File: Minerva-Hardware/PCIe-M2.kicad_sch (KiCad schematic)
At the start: 20 parts, among them J1 Bus_M.2_Socket_M, M6 M.2 Solder Nut, M7 M.2 Screw, U2 ASEK-32.768KHZ-L-R-T, U8 AP3441SHE-7B

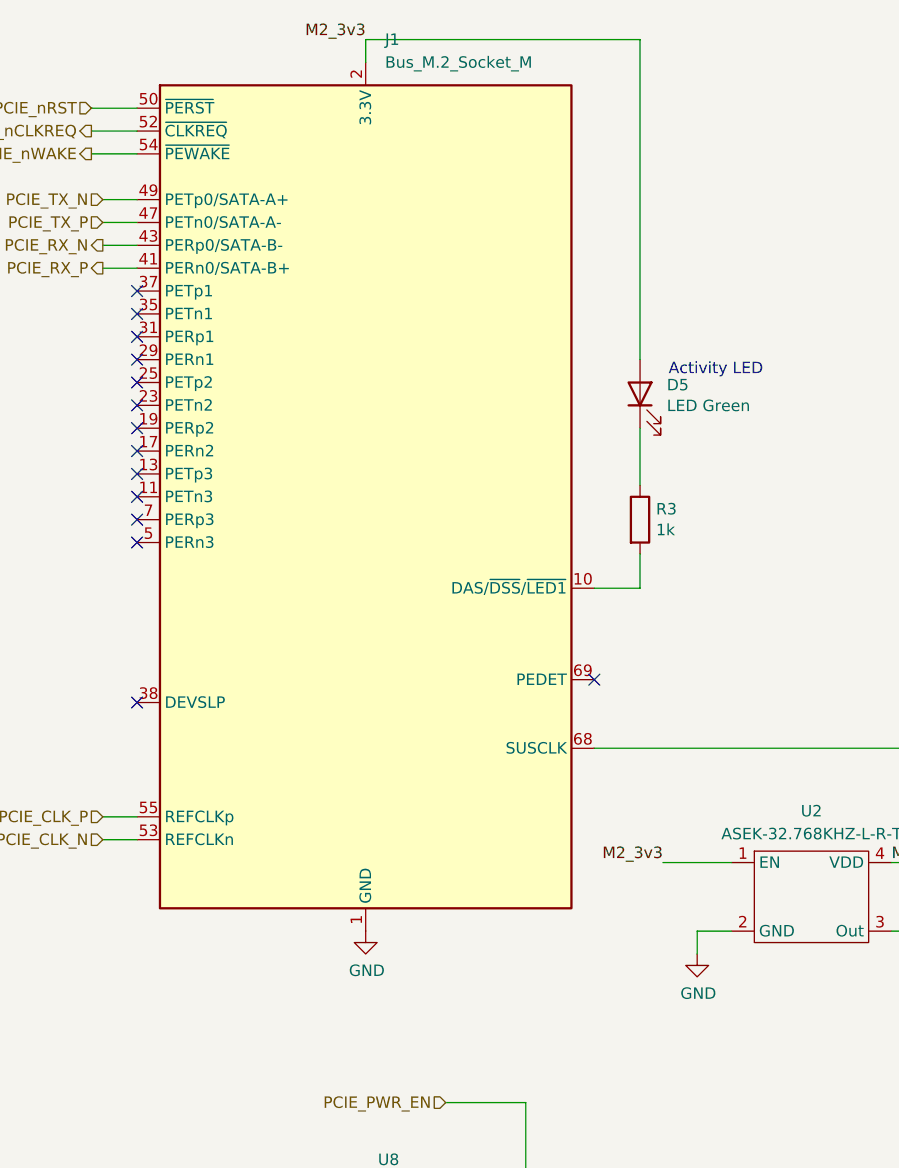
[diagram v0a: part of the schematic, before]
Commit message: Rename and commit actions due to mishap of location naming/saving
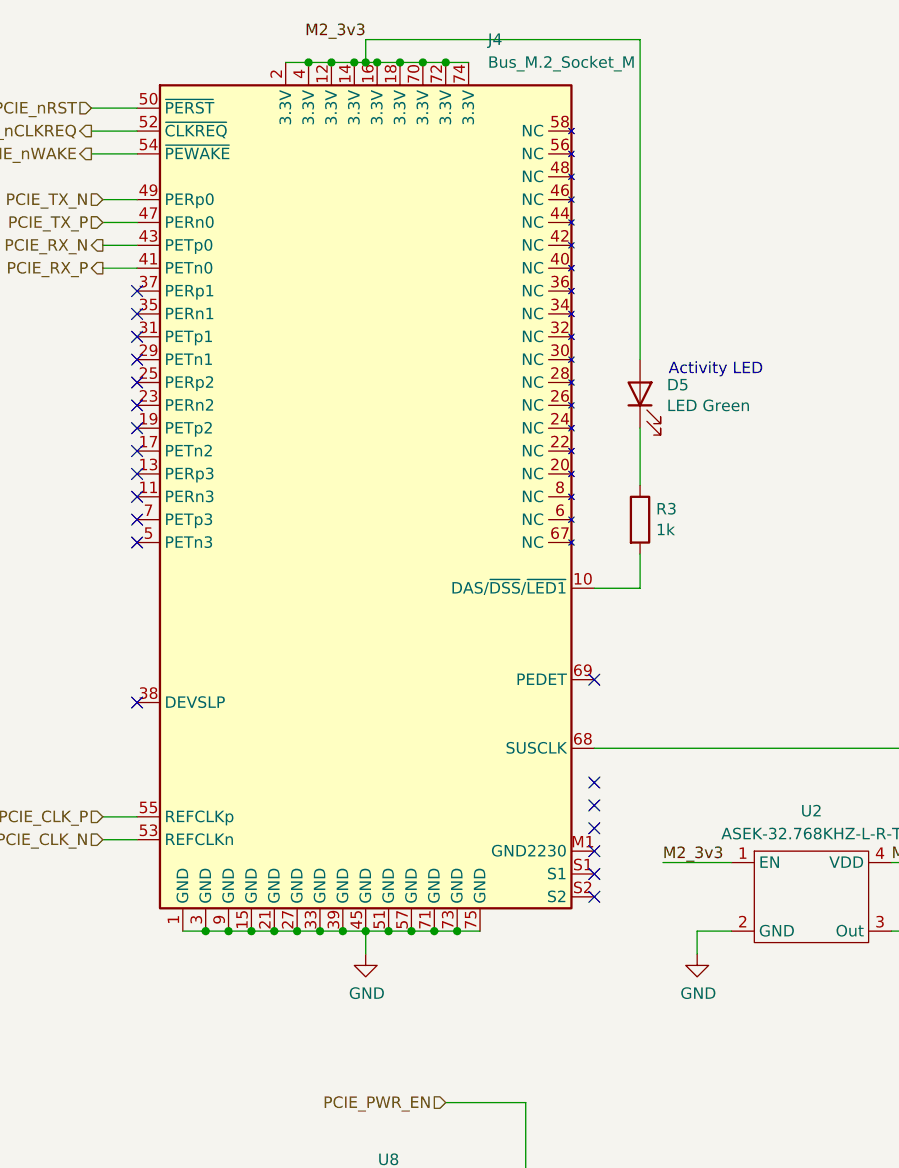
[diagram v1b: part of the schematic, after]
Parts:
- removed J1: Bus_M.2_Socket_M, Connector_PCBEdge:M.2_2242-xx-M, symbol Connector:Bus_M.2_Socket_M
- added J4: Bus_M.2_Socket_M, CM5 IO Board-rev2:M.2 M Key socket 2230, symbol CM5IO:Bus_M.2_Socket_M
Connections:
- net GND: now also J4.1 (GND), J4.15 (GND), J4.21 (GND), J4.27 (GND), J4.3 (GND), J4.33 (GND), J4.39 (GND), J4.45 (GND), J4.51 (GND), J4.57 (GND), J4.71 (GND), J4.73 (GND), J4.75 (GND), J4.9 (GND)
- net M2_3v3: now also J4.12 (3.3V), J4.14 (3.3V), J4.16 (3.3V), J4.18 (3.3V), J4.2 (3.3V), J4.4 (3.3V), J4.70 (3.3V), J4.72 (3.3V), J4.74 (3.3V)
- net PCIE_CLK_N: now also J4.53 (REFCLKn)
- net PCIE_CLK_P: now also J4.55 (REFCLKp)
- net PCIE_RX_N: now also J4.43 (PETp0)
- net PCIE_RX_P: now also J4.41 (PETn0)
- net PCIE_TX_N: now also J4.49 (PERp0)
- net PCIE_TX_P: now also J4.47 (PERn0)
- net PCIE_nCLKREQ: now also J4.52 (~{CLKREQ})
- net PCIE_nRST: now also J4.50 (~{PERST})
- net PCIE_nWAKE: now also J4.54 (~{PEWAKE})
- net at R3.2: now also J4.10 (DAS/~{DSS}/~{LED1})
- net at U2.3 (Out): now also J4.68 (SUSCLK)
- no-connect marks 15 -> 21

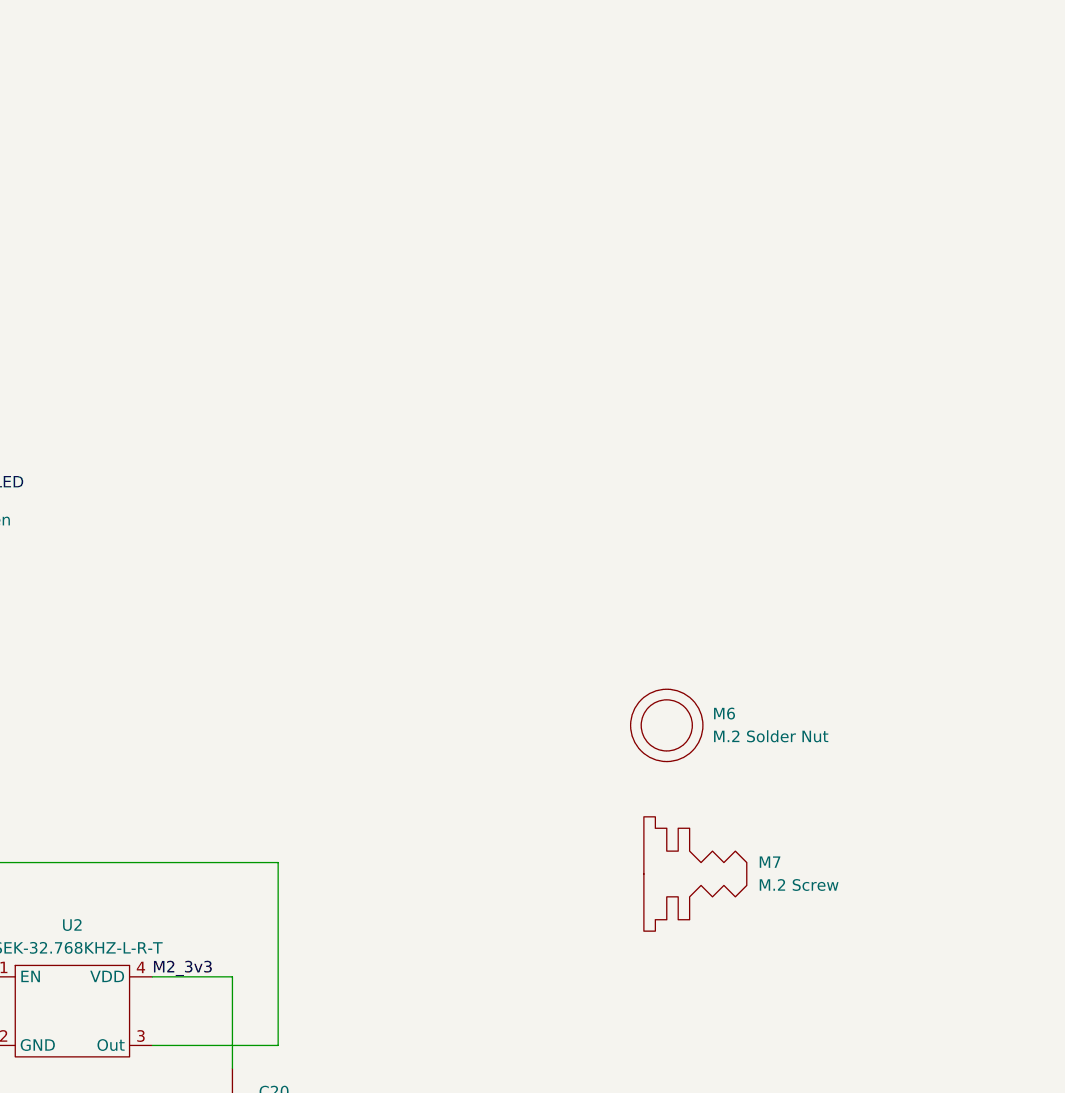
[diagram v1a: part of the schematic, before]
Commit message: Adding MiniPCI-E stuff
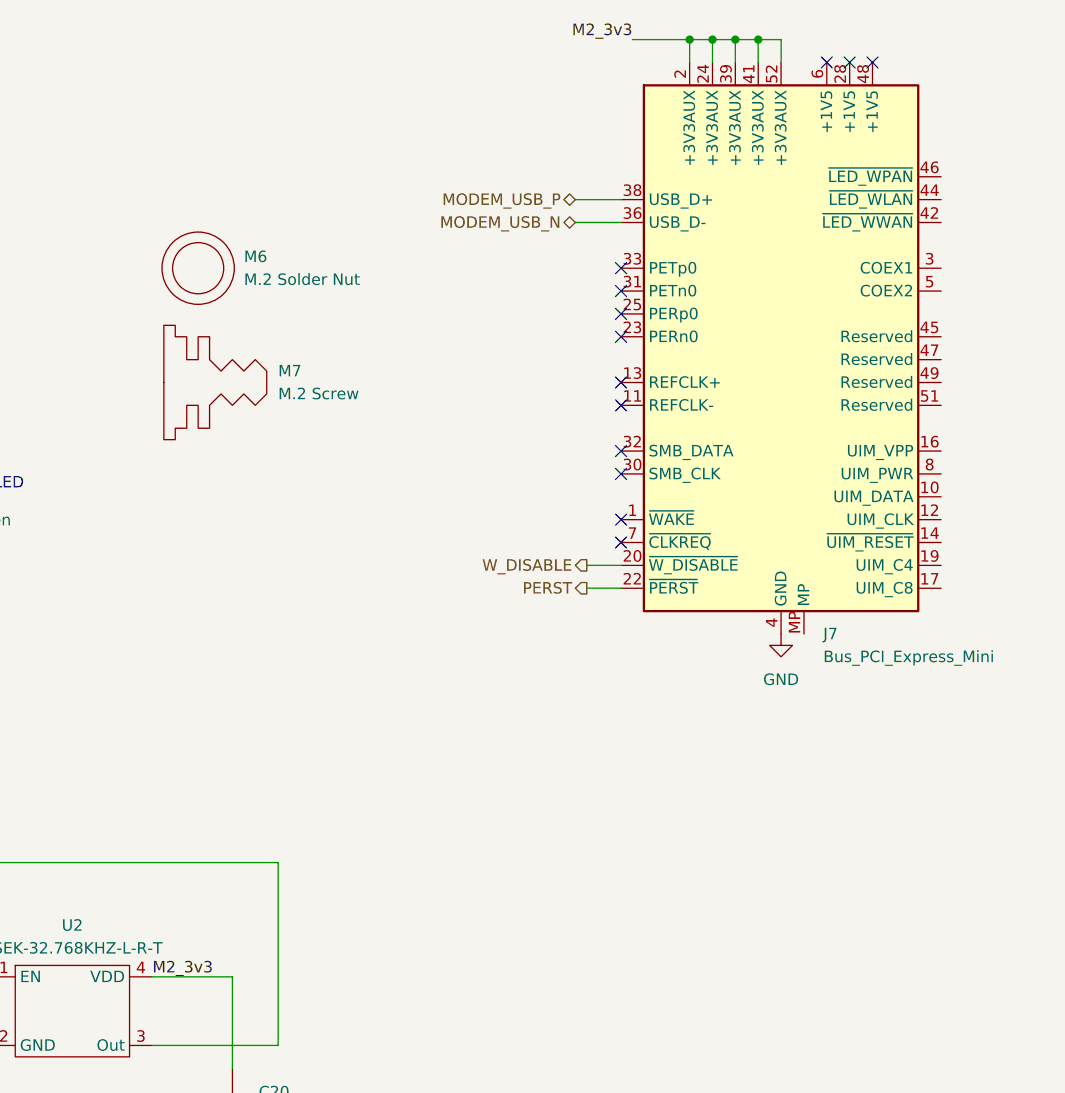
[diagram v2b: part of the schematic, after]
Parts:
- added J7: Bus_PCI_Express_Mini, symbol Connector:Bus_PCI_Express_Mini
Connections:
- net GND: now also J7.15 (GND), J7.18 (GND), J7.21 (GND), J7.26 (GND), J7.27 (GND), J7.29 (GND), J7.34 (GND), J7.35 (GND), J7.37 (GND), J7.4 (GND), J7.40 (GND), J7.43 (GND), J7.50 (GND), J7.9 (GND)
- net M2_3v3: now also J7.2 (+3V3AUX), J7.24 (+3V3AUX), J7.39 (+3V3AUX), J7.41 (+3V3AUX), J7.52 (+3V3AUX)
- new net MODEM_USB_N: J7.36 (USB_D-)
- new net MODEM_USB_P: J7.38 (USB_D+)
- new net PERST: J7.22 (~{PERST})
- new net W_DISABLE: J7.20 (~{W_DISABLE})
- no-connect marks 21 -> 34
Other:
- moved on the sheet: M6, M7

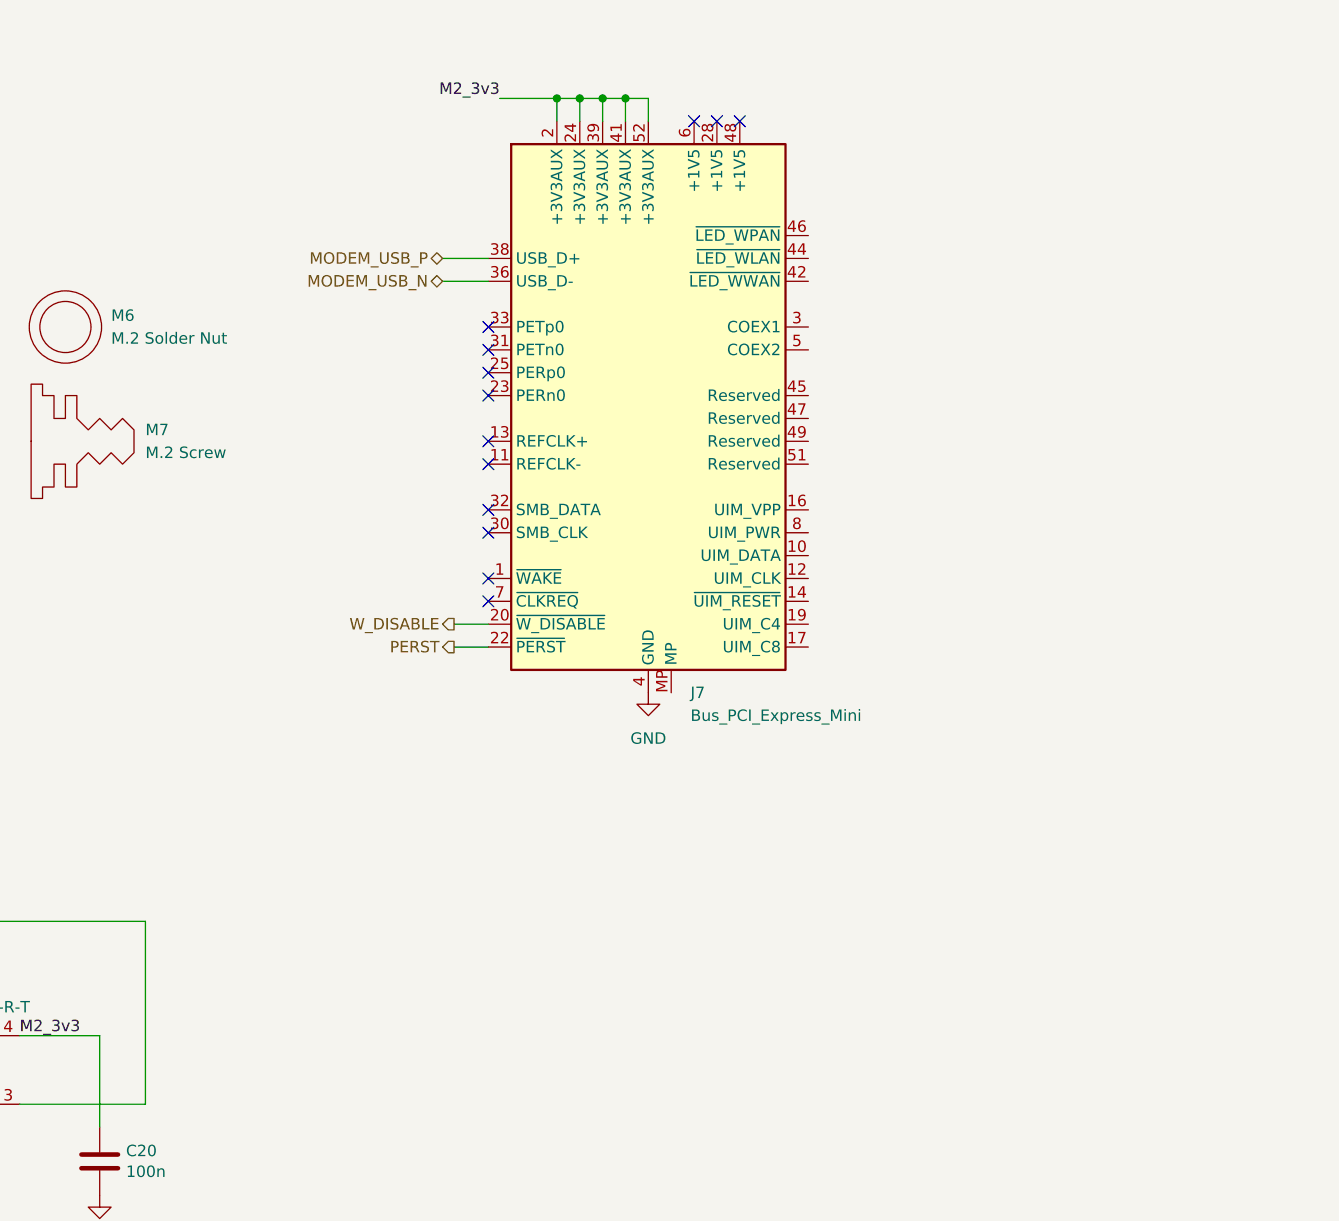
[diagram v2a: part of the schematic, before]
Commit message: Adding in the M.2 B WWAN
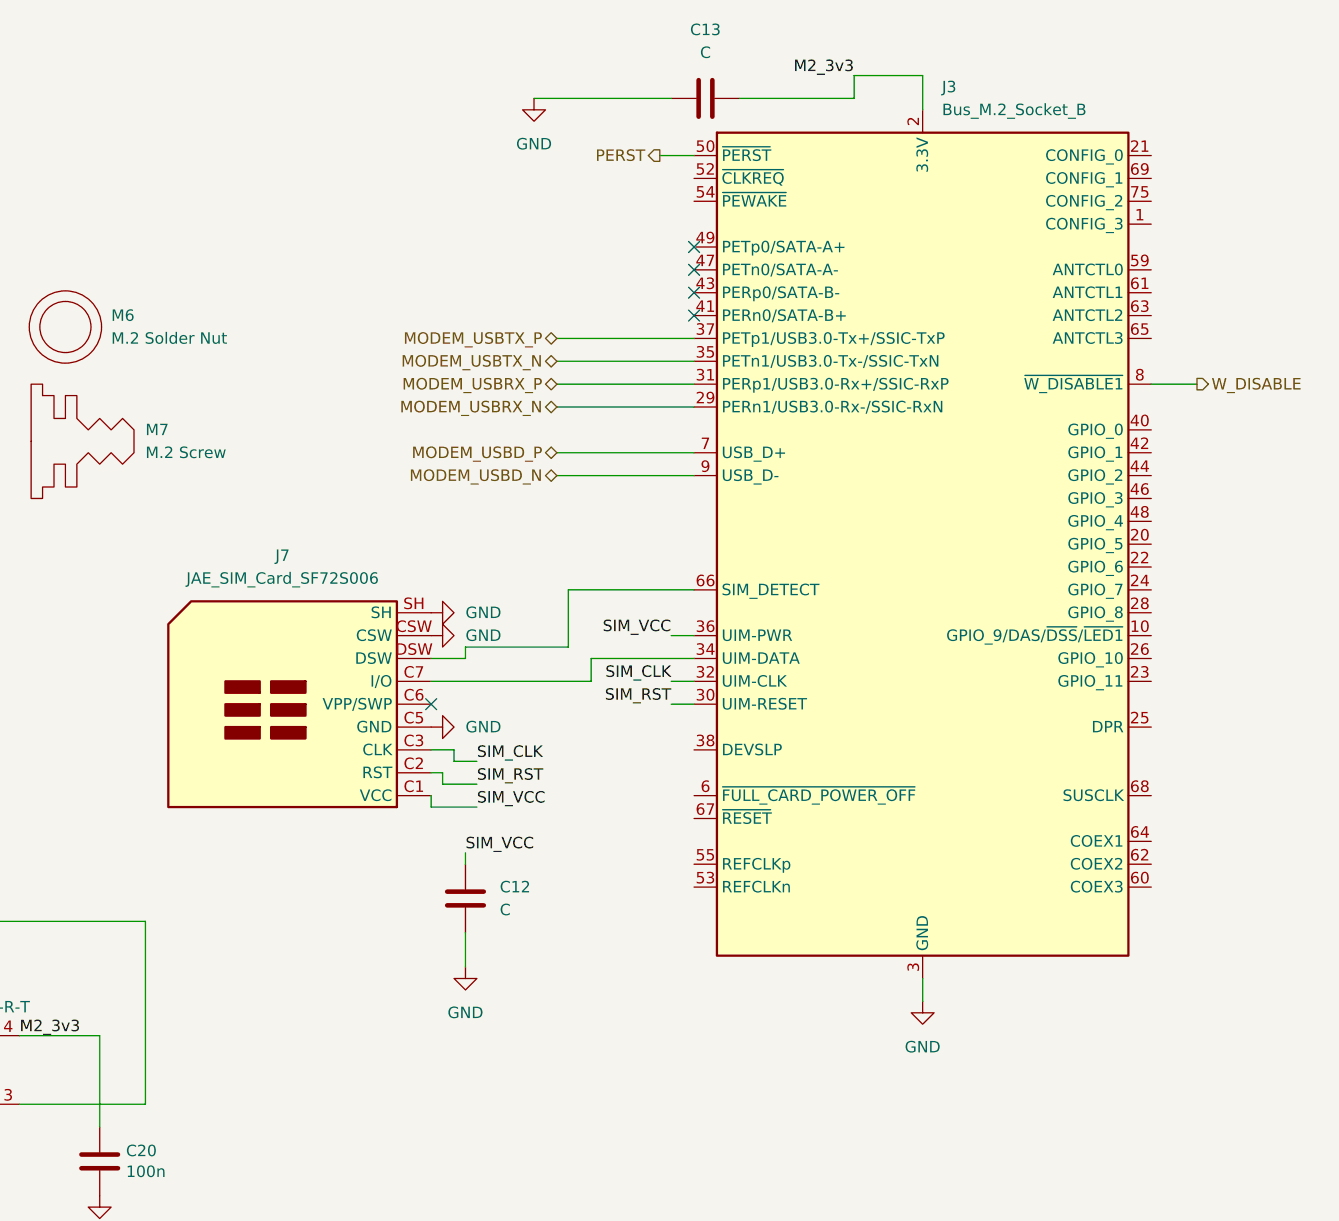
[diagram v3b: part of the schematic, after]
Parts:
- removed J7: Bus_PCI_Express_Mini, symbol Connector:Bus_PCI_Express_Mini
- added C12, C13: C, symbol Device:C
- added J3: Bus_M.2_Socket_B, Connector_PCBEdge:M.2_3042-xx-B, symbol Connector:Bus_M.2_Socket_B
- added J7: JAE_SIM_Card_SF72S006, Connector_JAE:JAE_SIM_Card_SF72S006, symbol Connector:JAE_SIM_Card_SF72S006
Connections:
- net GND: now also C12.2, C13.1, J3.11 (GND), J3.27 (GND), J3.3 (GND), J3.33 (GND), J3.39 (GND), J3.45 (GND), J3.5 (GND), J3.51 (GND), J3.57 (GND), J3.71 (GND), J3.73 (GND), J7.C5 (GND), J7.CSW, J7.SH
- net M2_3v3: now also C13.2, J3.2 (3.3V), J3.4 (3.3V), J3.70 (3.3V), J3.72 (3.3V), J3.74 (3.3V)
- net PERST: now also J3.50 (~{PERST})
- net W_DISABLE: now also J3.8 (~{W_DISABLE1})
- new net: J3.34 (UIM-DATA), J7.C7 (I/O)
- new net: J3.66 (SIM_DETECT), J7.DSW
- new net MODEM_USBD_N: J3.9 (USB_D-)
- new net MODEM_USBD_P: J3.7 (USB_D+)
- new net MODEM_USBRX_N: J3.29 (PERn1/USB3.0-Rx-/SSIC-RxN)
- new net MODEM_USBRX_P: J3.31 (PERp1/USB3.0-Rx+/SSIC-RxP)
- new net MODEM_USBTX_N: J3.35 (PETn1/USB3.0-Tx-/SSIC-TxN)
- new net MODEM_USBTX_P: J3.37 (PETp1/USB3.0-Tx+/SSIC-TxP)
- new net SIM_CLK: J3.32 (UIM-CLK), J7.C3 (CLK)
- new net SIM_RST: J3.30 (UIM-RESET), J7.C2 (RST)
- new net SIM_VCC: C12.1, J3.36 (UIM-PWR), J7.C1 (VCC)
- no-connect marks 34 -> 26

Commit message: Redid the BQ powerpath unit
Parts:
- J3: footprint Connector_PCBEdge:M.2_3042-xx-B -> M.2B:CONN67_2199230_TEC
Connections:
- no-connect marks 26 -> 48
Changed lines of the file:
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@@
 	)
 	(no_connect
+		(at 255.27 63.5)
+	)
+	(no_connect
 		(at 64.77 165.1)
 	)
@@
 	)
 	(no_connect
+		(at 255.27 68.58)
+	)
+	(no_connect
+		(at 255.27 101.6)
+	)
+	(no_connect
 		(at 96.52 116.84)
 	)
@@
 	)
 	(no_connect
+		(at 255.27 38.1)
+	)
+	(no_connect
+		(at 255.27 66.04)
+	)
+	(no_connect
 		(at 175.26 86.36)
 	)
 	(no_connect
+		(at 255.27 81.28)
+	)
+	(no_connect
+		(at 255.27 43.18)
+	)
+	(no_connect
 		(at 96.52 114.3)
 	)
 	(no_connect
+		(at 255.27 73.66)
+	)
+	(no_connect
+		(at 204.47 106.68)
+	)
+	(no_connect
+		(at 255.27 40.64)
+	)
+	(no_connect
 		(at 45.72 82.55)
 	)
 	(no_connect
+		(at 255.27 60.96)
+	)
+	(no_connect
 		(at 45.72 69.85)
 	)
@@
 	)
 	(no_connect
+		(at 255.27 58.42)
+	)
+	(no_connect
+		(at 255.27 45.72)
+	)
+	(no_connect
 		(at 45.72 72.39)
 	)
@@
 	)
 	(no_connect
+		(at 255.27 71.12)
+	)
+	(no_connect
 		(at 204.47 35.56)
 	)
 	(no_connect
+		(at 255.27 106.68)
+	)
+	(no_connect
 		(at 45.72 64.77)
 	)
@@
 	)
 	(no_connect
+		(at 255.27 76.2)
+	)
+	(no_connect
 		(at 96.52 119.38)
 	)
 	(no_connect
+		(at 255.27 55.88)
+	)
+	(no_connect
 		(at 96.52 127)
 	)
@@
 	)
 	(no_connect
+		(at 204.47 30.48)
+	)
+	(no_connect
+		(at 255.27 83.82)
+	)
+	(no_connect
+		(at 255.27 104.14)
+	)
+	(no_connect
 		(at 96.52 102.87)
 	)
+	(no_connect
+		(at 204.47 104.14)
+	)
+	(no_connect
+		(at 204.47 27.94)
+	)
 	(wire
 		(pts
@@
 			)
 		)
-		(property "Footprint" "Connector_PCBEdge:M.2_3042-xx-B"
+		(property "Footprint" "M.2B:CONN67_2199230_TEC"
 			(at 229.87 41.91 0)
 			(hide yes)
